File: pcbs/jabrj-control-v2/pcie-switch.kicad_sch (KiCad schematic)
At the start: 90 parts, among them U1001 SYA75603A, U1002 PCI11010C, U1003 AT24C64D-MAHM-E, Y1001 XRCGB25M000F3A16R0

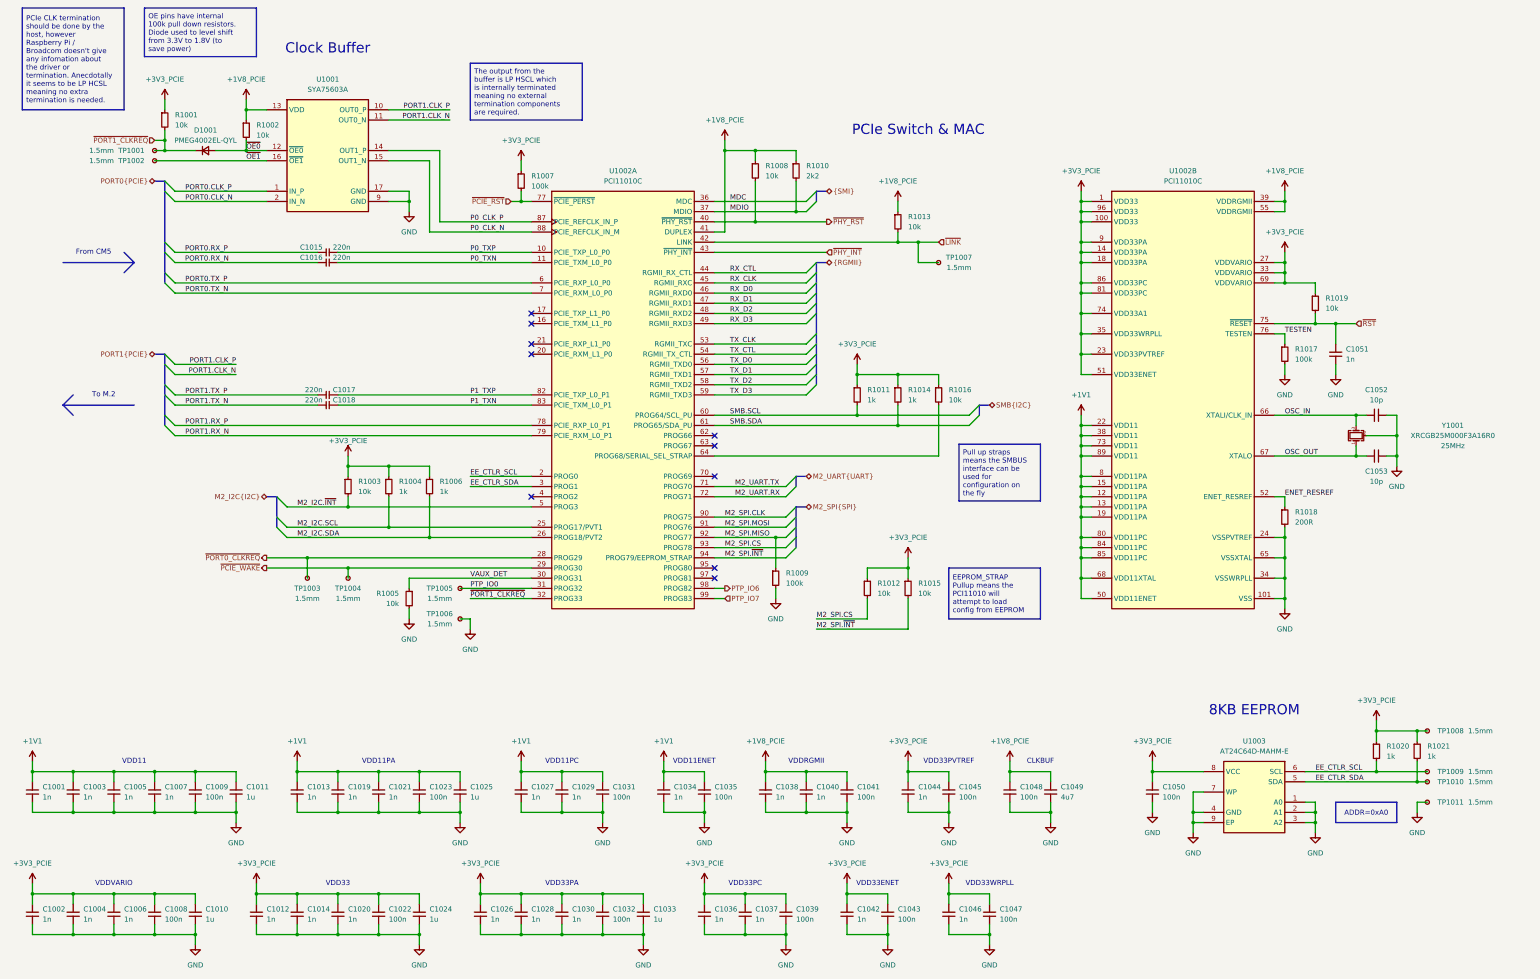
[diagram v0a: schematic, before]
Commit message: Fixed 5V buck inductor value
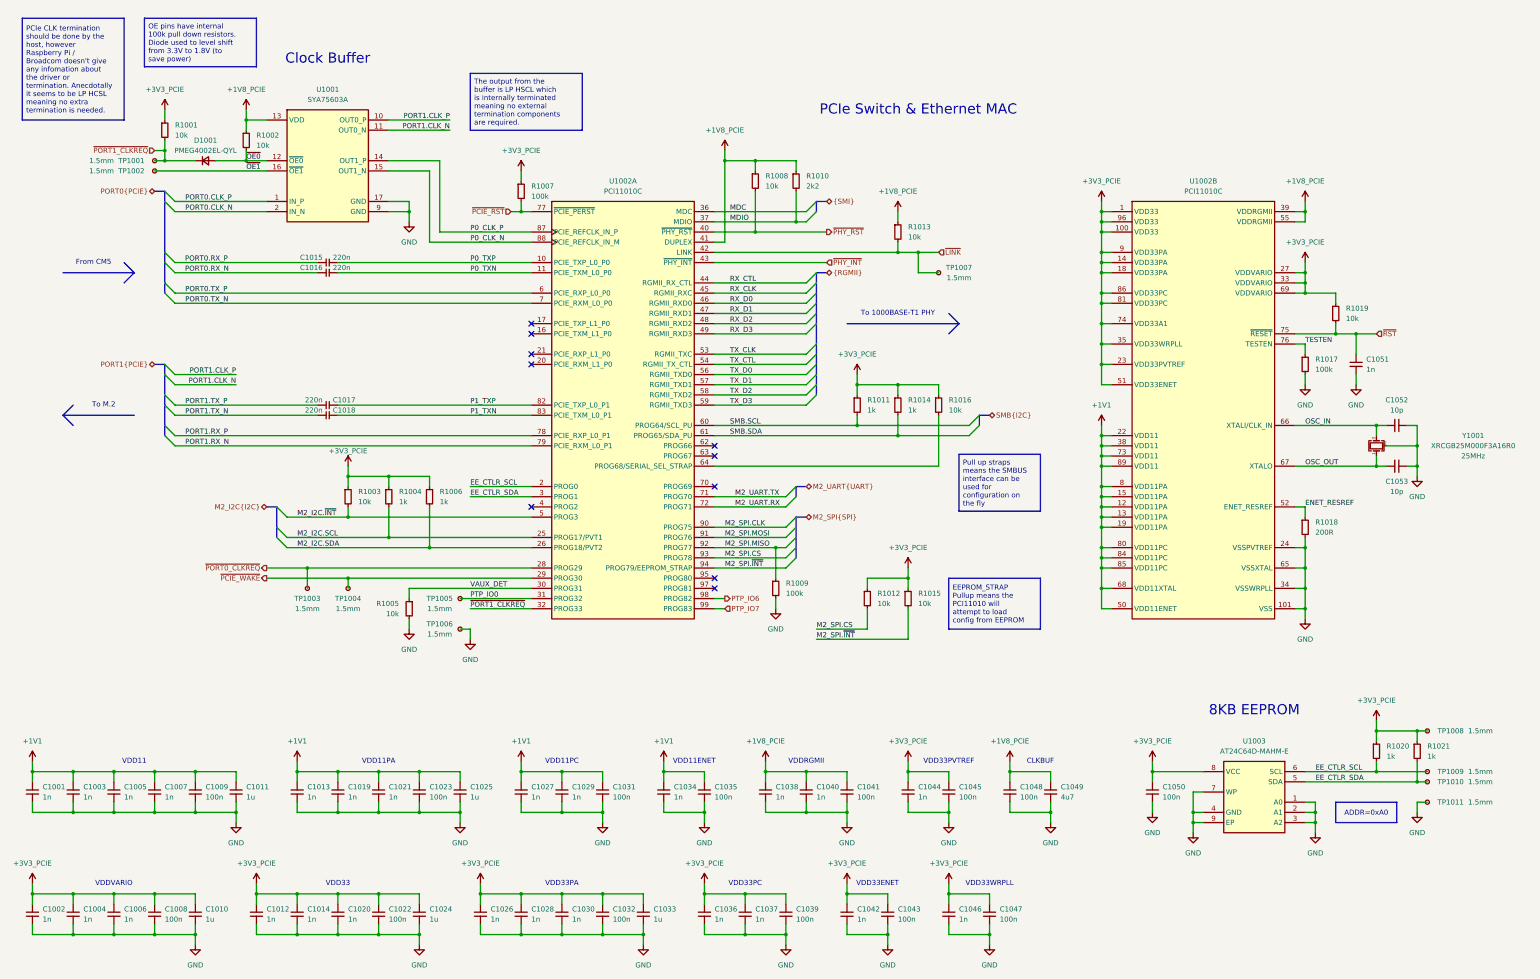
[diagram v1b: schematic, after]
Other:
- note added: "PCIe Switch & Ethernet MAC"
- note added: "To 1000BASE-T1 PHY"
- note removed: "PCIe Switch & MAC"
- moved on the sheet: C1015, C1016, C1017, C1018, C1051, C1052, C1053, D1001, R1001, R1002, R1003, R1004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

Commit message: Minor schematic fixes
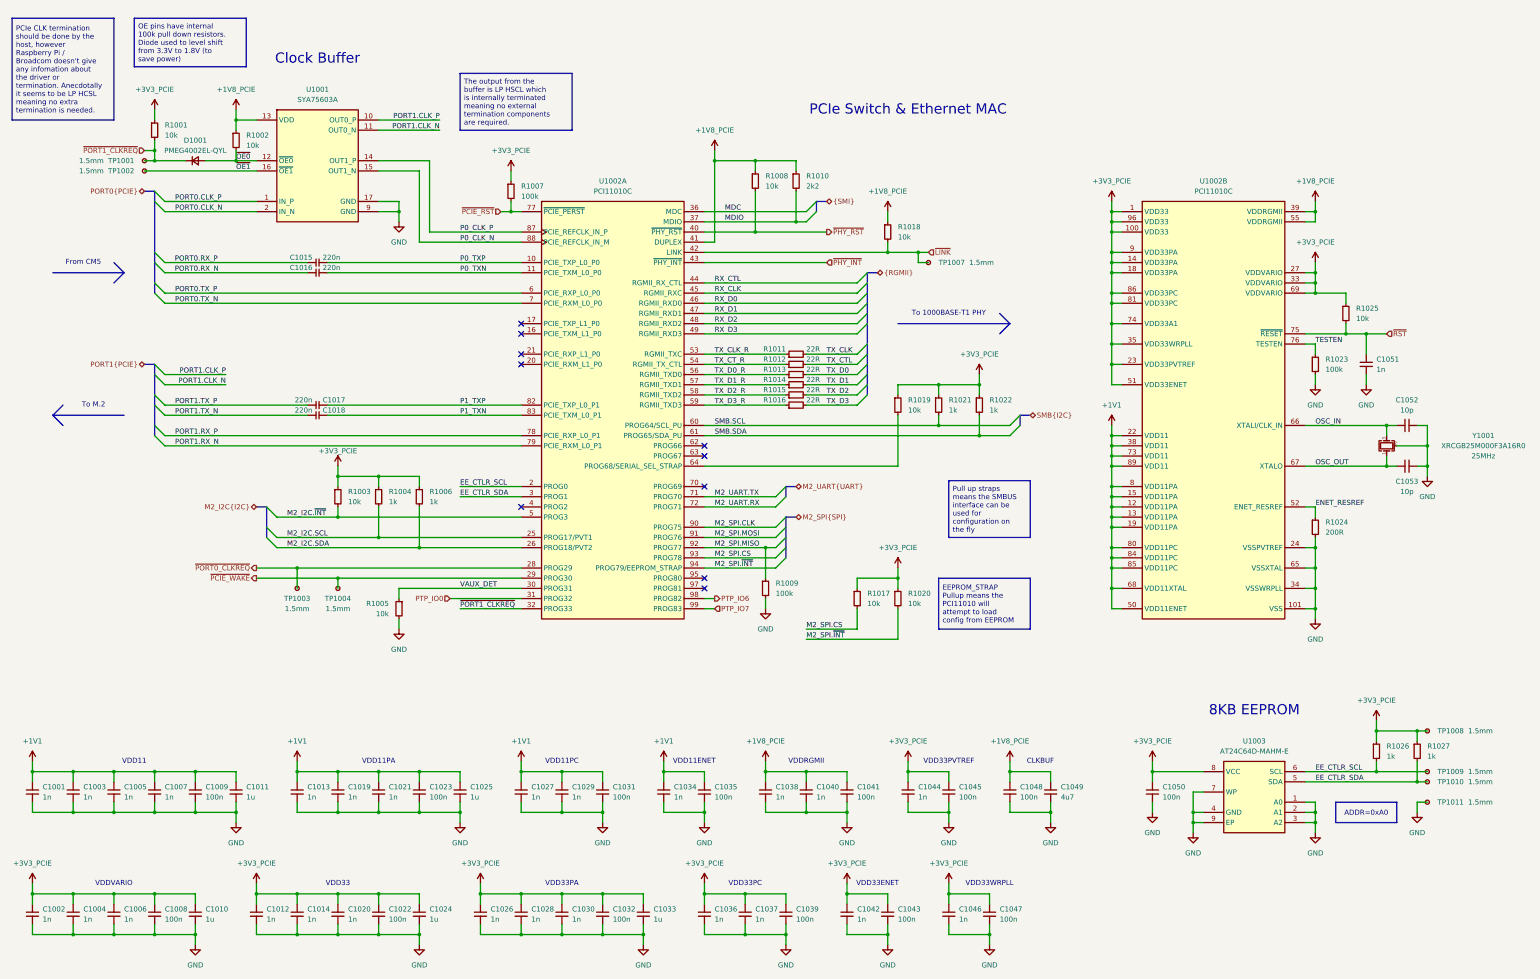
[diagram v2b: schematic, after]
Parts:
- removed TP1005, TP1006: 1.5mm, project_footprints:TestPoint_Pad_D1.5mm, symbol Connector:TestPoint_Small
- added R1011, R1012, R1013, R1014, R1015, R1016: 22R, project_footprints:R_0402, symbol Device:R_Small
- renumbered R1012 to R1017, R1013 to R1018, R1016 to R1019, R1015 to R1020, R1011 to R1021, R1014 to R1022, R1017 to R1023, R1018 to R1024, R1019 to R1025, R1020 to R1026, R1021 to R1027
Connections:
- net TX_CLK: now also R1011.2; no longer U1002.53 (PROG58)
- net TX_CTL: now also R1012.2; no longer U1002.54 (PROG59)
- net TX_D0: now also R1013.2; no longer U1002.56 (PROG60)
- net TX_D1: now also R1014.2; no longer U1002.57 (PROG61)
- net TX_D2: now also R1015.2; no longer U1002.58 (PROG62)
- net TX_D3: now also R1016.2; no longer U1002.59 (PROG63)
- new net TX_CLK_R: R1011.1, U1002.53 (PROG58)
- new net TX_CT_R: R1012.1, U1002.54 (PROG59)
- new net TX_D0_R: R1013.1, U1002.56 (PROG60)
- new net TX_D1_R: R1014.1, U1002.57 (PROG61)
- new net TX_D2_R: R1015.1, U1002.58 (PROG62)
- new net TX_D3_R: R1016.1, U1002.59 (PROG63)
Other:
- moved on the sheet: C1015, C1016, C1017, C1018, C1051, C1052, C1053, D1001, R1001, R1002, R1003, R1004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

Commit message: 895 Unrouted
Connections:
- net P1_TXN: now also C1017.1, U1002.82 (PCIE_TXP_L0_P1); no longer C1018.1, U1002.83 (PCIE_TXM_L0_P1)
- net P1_TXP: now also C1018.1, U1002.83 (PCIE_TXM_L0_P1); no longer C1017.1, U1002.82 (PCIE_TXP_L0_P1)
- net PORT1.CLK_N: now also U1001.10 (OUT0_P); no longer U1001.11 (OUT0_N)
- net PORT1.CLK_P: now also U1001.11 (OUT0_N); no longer U1001.10 (OUT0_P)
- net PORT1.RX_N: now also U1002.78 (PCIE_RXP_L0_P1); no longer U1002.79 (PCIE_RXM_L0_P1)
- net PORT1.RX_P: now also U1002.79 (PCIE_RXM_L0_P1); no longer U1002.78 (PCIE_RXP_L0_P1)
- net PORT1.TX_N: now also C1017.2; no longer C1018.2
- net PORT1.TX_P: now also C1018.2; no longer C1017.2
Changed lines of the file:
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@@
 		)
 	)
+	(text_box "P/N swapping to ease routing"
+		(exclude_from_sim no)
+		(at 114.3 121.0071 0)
+		(size 17.78 5.9929)
+		(margins 0.9525 0.9525 0.9525 0.9525)
+		(stroke
+			(width 0)
+			(type solid)
+		)
+		(fill
+			(type none)
+		)
+		(effects
+			(font
+				(size 1.27 1.27)
+			)
+			(justify left)
+		)
+	)
 	(text_box "The output from the buffer is LP HSCL which is internally terminated meaning no external termination components are required."
 		(exclude_from_sim no)
-		(at 134.62 46.7886 0)
+		(at 137.16 45.72 0)
 		(size 27.94 14.1714)
 		(margins 0.9525 0.9525 0.9525 0.9525)
@@
 		)
 	)
+	(text_box "P/N swapping to ease routing"
+		(exclude_from_sim no)
+		(at 114.3 45.72 0)
+		(size 17.78 5.9929)
+		(margins 0.9525 0.9525 0.9525 0.9525)
+		(stroke
+			(width 0)
+			(type solid)
+		)
+		(fill
+			(type none)
+		)
+		(effects
+			(font
+				(size 1.27 1.27)
+			)
+			(justify left)
+		)
+	)
 	(text_box "ADDR=0xA0"
 		(exclude_from_sim no)
@@
 	)
 	(junction
+		(at 124.46 147.32)
+		(diameter 0)
+		(color 0 0 0 0)
+	)
+	(junction
 		(at 241.3 91.44)
 		(diameter 0)
@@
 	)
 	(junction
-		(at 104.14 147.32)
-		(diameter 0)
-		(color 0 0 0 0)
-	)
-	(junction
 		(at 297.18 160.02)
 		(diameter 0)
@@
 	(wire
 		(pts
-			(xy 124.46 147.32) (xy 114.3 147.32)
-		)
-		(stroke
-			(width 0)
-			(type default)
-		)
-	)
-	(wire
-		(pts
 			(xy 347.98 175.26) (xy 347.98 180.34)
 		)
@@
 	(wire
 		(pts
-			(xy 114.3 147.32) (xy 104.14 147.32)
-		)
-		(stroke
-			(width 0)
-			(type default)
-		)
-	)
-	(wire
-		(pts
 			(xy 373.38 134.62) (xy 375.92 134.62)
 		)
@@
 	(wire
 		(pts
-			(xy 104.14 144.78) (xy 104.14 147.32)
+			(xy 124.46 144.78) (xy 124.46 147.32)
 		)
 		(stroke
@@
 	(wire
 		(pts
+			(xy 104.14 147.32) (xy 124.46 147.32)
+		)
+		(stroke
+			(width 0)
+			(type default)
+		)
+	)
+	(wire
+		(pts
 			(xy 355.6 111.76) (xy 360.68 111.76)
 		)
@@
 	)
 	(label "PORT1.RX_P"
-		(at 63.5 137.16 0)
+		(at 63.5 139.7 0)
 		(effects
 			(font
@@
 	)
 	(label "PORT1.RX_N"
-		(at 63.5 139.7 0)
+		(at 63.5 137.16 0)
 		(effects
 			(font
@@
 	)
 	(label "P1_TXN"
-		(at 134.62 132.08 0)
+		(at 134.62 129.54 0)
 		(effects
 			(font
@@
 	)
 	(label "PORT1.TX_N"
-		(at 63.5 132.08 0)
+		(at 63.5 129.54 0)
 		(effects
 			(font
@@
 	)
 	(label "PORT1.TX_P"
-		(at 63.5 129.54 0)
+		(at 63.5 132.08 0)
 		(effects
 			(font
@@
 	)
 	(label "P1_TXP"
-		(at 134.62 129.54 0)
+		(at 134.62 132.08 0)
 		(effects
 			(font
@@
 	)
 	(label "PORT1.CLK_N"
-		(at 129.54 60.96 180)
+		(at 129.54 58.42 180)
 		(effects
 			(font
@@
 	)
 	(label "PORT1.CLK_P"
-		(at 129.54 58.42 180)
+		(at 129.54 60.96 180)
 		(effects
 			(font
@@
 		(polyline
 			(pts
-				(xy 109.22 127) (xy 111.76 127) (xy 111.76 134.62) (xy 109.22 134.62)
+				(xy 88.9 124.46) (xy 109.22 124.46) (xy 109.22 142.24) (xy 88.9 142.24)
 			)
 			(stroke
@@
 		(polyline
 			(pts
-				(xy 109.22 91.44) (xy 111.76 91.44) (xy 111.76 99.06) (xy 109.22 99.06)
+				(xy 116.84 66.04) (xy 119.38 66.04) (xy 119.38 73.66) (xy 116.84 73.66)
+			)
+			(stroke
+				(width 0)
+				(type dash)
+			)
+			(fill
+				(type none)
+			)
+		)
+	)
+	(rule_area
+		(exclude_from_sim no)
+		(in_bom yes)
+		(on_board yes)
+		(dnp no)
+		(polyline
+			(pts
+				(xy 88.9 88.9) (xy 109.22 88.9) (xy 109.22 106.68) (xy 88.9 106.68)
+			)
+			(stroke
+				(width 0)
+				(type dash)
+			)
+			(fill
+				(type none)
+			)
+		)
+	)
+	(rule_area
+		(exclude_from_sim no)
+		(in_bom yes)
+		(on_board yes)
+		(dnp no)
+		(polyline
+			(pts
+				(xy 196.85 113.665) (xy 208.28 113.665) (xy 208.28 130.81) (xy 196.85 130.81)
 			)
 			(stroke
@@
 		(length 2.54)
 		(shape round)
-		(at 58.42 76.2 0)
+		(at 58.42 119.38 0)
 		(fields_autoplaced yes)
 		(effects
@@
 			(justify left bottom)
 		)
-		(property "Net Class" "PCIe"
-			(at 59.1185 73.66 0)
+		(property "Net Class" "PCIe (85Ω)"
+			(at 59.1185 116.84 0)
 			(show_name no)
 			(do_not_autoplace no)
@@
 		)
 		(property "Component Class" ""
-			(at 58.42 66.04 0)
+			(at -111.76 208.28 0)
 			(show_name no)
 			(do_not_autoplace no)
@@
 		(length 2.54)
 		(shape round)
-		(at 58.42 119.38 0)
+		(at 88.9 142.24 180)
 		(fields_autoplaced yes)
 		(effects
@@
 				(size 1.27 1.27)
 			)
-			(justify left bottom)
+			(justify right bottom)
 		)
-		(property "Net Class" "PCIe"
-			(at 59.1185 116.84 0)
+		(property "Net Class" "PCIe (85Ω)"
+			(at 89.5985 144.78 0)
+			(show_name no)
+			(do_not_autoplace no)
+			(effects
+				(font
+					(size 1.27 1.27)
+				)
+				(justify left)
+			)
+		)
+		(property "Component Class" ""
+			(at -81.28 231.14 0)
+			(show_name no)
+			(do_not_autoplace no)
+			(effects
+				(font
+					(size 1.27 1.27)
+					(italic yes)
+				)
+			)
+		)
+	)
+	(netclass_flag ""
+		(length 2.54)
+		(shape round)
+		(at 88.9 106.68 180)
+		(fields_autoplaced yes)
+		(effects
+			(font
+				(size 1.27 1.27)
+			)
+			(justify right bottom)
+		)
+		(property "Net Class" "PCIe (90Ω)"
+			(at 89.5985 109.22 0)
+			(show_name no)
+			(do_not_autoplace no)
+			(effects
+				(font
+					(size 1.27 1.27)
+				)
+				(justify left)
+			)
+		)
+		(property "Component Class" ""
+			(at -71.12 205.74 0)
+			(show_name no)
+			(do_not_autoplace no)
+			(effects
+				(font
+					(size 1.27 1.27)
+					(italic yes)
+				)
+			)
+		)
+	)
+	(netclass_flag ""
+		(length 2.54)
+		(shape round)
+		(at 208.28 130.81 180)
+		(fields_autoplaced yes)
+		(effects
+			(font
+				(size 1.27 1.27)
+			)
+			(justify right bottom)
+		)
+		(property "Net Class" "xMII"
+			(at 208.9785 133.35 0)
 			(show_name no)
 			(do_not_autoplace no)
@@
 		)
 		(property "Component Class" ""
-			(at 58.42 109.22 0)
+			(at -210.82 173.99 0)
 			(show_name no)
 			(do_not_autoplace no)
@@
 					(italic yes)
 				)
+				(justify left)
 			)
 		)
@@
 		(length 2.54)
 		(shape round)
-		(at 109.22 127 0)
+		(at 58.42 76.2 0)
 		(fields_autoplaced yes)
 		(effects
@@
 			(justify left bottom)
 		)
-		(property "Net Class" "PCIe"
-			(at 109.9185 124.46 0)
+		(property "Net Class" "PCIe (90Ω)"
+			(at 59.1185 73.66 0)
 			(show_name no)
 			(do_not_autoplace no)
@@
 		)
 		(property "Component Class" ""
-			(at 109.22 116.84 0)
+			(at -71.12 10.16 0)
 			(show_name no)
 			(do_not_autoplace no)
@@
 		(length 2.54)
 		(shape round)
-		(at 109.22 91.44 0)
+		(at 116.84 66.04 0)
 		(fields_autoplaced yes)
 		(effects
@@
 			(justify left bottom)
 		)
-		(property "Net Class" "PCIe"
-			(at 109.9185 88.9 0)
+		(property "Net Class" "PCIe (85Ω)"
+			(at 117.5385 63.5 0)
 			(show_name no)
 			(do_not_autoplace no)
@@
 		)
 		(property "Component Class" ""
-			(at 109.22 81.28 0)
+			(at -53.34 154.94 0)
 			(show_name no)
 			(do_not_autoplace no)
@@
 	(symbol
 		(lib_id "PWR-SYM:+3V3_PCIE")
-		(at 104.14 144.78 0)
+		(at 124.46 144.78 0)
 		(unit 1)
 		(body_style 1)
@@
 		(dnp no)
 		(property "Reference" "#PWR01009"
-			(at 104.14 148.59 0)
+			(at 124.46 148.59 0)
 			(hide yes)
 			(show_name no)
@@
 		)
 		(property "Value" "+3V3_PCIE"
-			(at 104.14 140.97 0)
+			(at 124.46 140.97 0)
 			(show_name no)
 			(do_not_autoplace no)
@@
 		)
 		(property "Footprint" ""
-			(at 104.14 144.78 0)
+			(at 124.46 144.78 0)
 			(hide yes)
 			(show_name no)
@@
 		)
 		(property "Datasheet" ""
-			(at 104.14 144.78 0)
+			(at 124.46 144.78 0)
 			(hide yes)
 			(show_name no)
@@
 		)
 		(property "Description" "Power symbol creates a global label with name \"+3V3_PCIE\""
-			(at 104.14 144.78 0)
+			(at 124.46 144.78 0)
 			(hide yes)
 			(show_name no)
